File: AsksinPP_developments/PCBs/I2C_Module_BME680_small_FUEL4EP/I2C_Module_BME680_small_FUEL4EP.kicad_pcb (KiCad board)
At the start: 2 copper layers, 14.1 x 17 mm, 11 parts, among them J1 Conn_01x04, U1 BME680

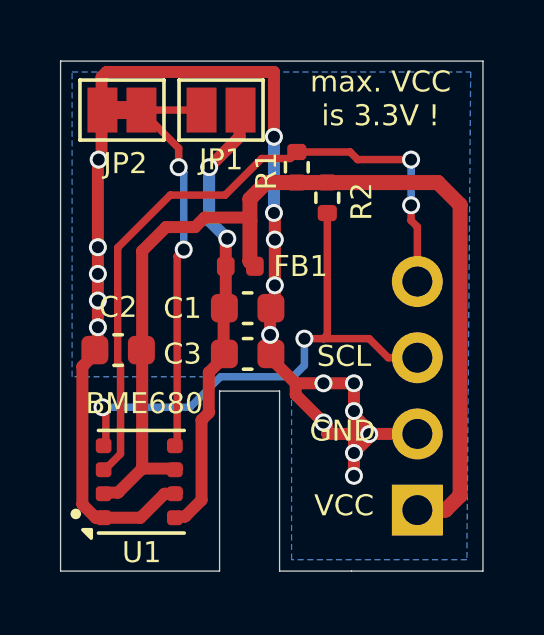
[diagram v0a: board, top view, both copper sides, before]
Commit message: PCBs: migration to KiCAD8 / PCBs/I2C_Module_BME680_small_FUEL4EP: improved VDDA decoupling
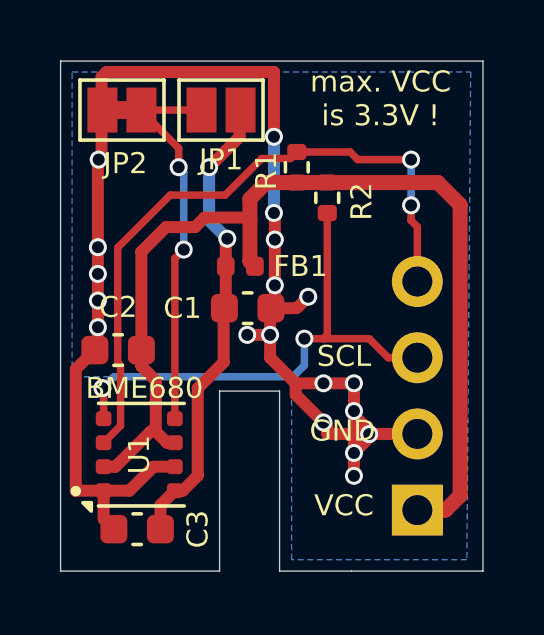
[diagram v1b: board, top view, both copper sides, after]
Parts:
- moved C3 6.91 mm to (2.55, -1.40), turned to 0 degrees
- moved U1 0.90 mm to (2.62, -3.88)
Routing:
- net GND: track 47.0 -> 49.7 mm, vias 17 -> 19
- net Net-(JP1-A): track 13.8 -> 13.0 mm
- net /SDA: track 23.0 -> 22.1 mm
- net VCC: track 35.2 -> 34.5 mm
- net VDDA: track 15.0 -> 15.6 mm
- net /SCL: track 17.8 -> 17.2 mm
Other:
- board text added: "BME680 I2C Modul small (C) FUEL4EP V1.1 09/2024"
- board text removed: "BME680 I2C Modul small (C) FUEL4EP V1.0 09/2024"

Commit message: PCBs: updated some JLCPCB manufacturing data after trial-order
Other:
- board text added: "JLCJLCJLCJLC"
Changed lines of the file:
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@@
 		(sheetfile "I2C_Module_BME680_small_FUEL4EP.kicad_sch")
 		(zone_connect 1)
-		(attr exclude_from_pos_files)
+		(attr exclude_from_pos_files exclude_from_bom)
 		(fp_line
 			(start -1.4 -1)
@@
 		(sheetfile "I2C_Module_BME680_small_FUEL4EP.kicad_sch")
 		(zone_connect 1)
-		(attr exclude_from_pos_files)
+		(attr exclude_from_pos_files exclude_from_bom)
 		(net_tie_pad_groups "1, 2")
 		(fp_poly
@@
 		)
 		(property "Value" "100n"
-			(at 0 1.43 360)
+			(at 0 1.43 0)
 			(layer "F.Fab")
 			(effects
@@
 		)
 		(fp_text user "${REFERENCE}"
-			(at 0 0 360)
+			(at 0 0 0)
 			(layer "F.Fab")
 			(effects
@@
 		(sheetname "Stammblatt")
 		(sheetfile "I2C_Module_BME680_small_FUEL4EP.kicad_sch")
-		(attr through_hole exclude_from_pos_files)
+		(attr through_hole exclude_from_pos_files exclude_from_bom)
 		(fp_line
 			(start -1.33 -8.95)
@@
 			(size 1.7 1.7)
 			(drill 1)
-			(layers "*.Cu" "*.Mask")
+			(layers "*.Cu" "*.Mask" "In1.Cu" "In2.Cu" "In3.Cu" "In4.Cu" "In5.Cu" "In6.Cu"
+				"In7.Cu" "In8.Cu" "In9.Cu" "In10.Cu" "In11.Cu" "In12.Cu" "In13.Cu" "In14.Cu"
+				"In15.Cu" "In16.Cu" "In17.Cu" "In18.Cu" "In19.Cu" "In20.Cu" "In21.Cu"
+				"In22.Cu" "In23.Cu" "In24.Cu" "In25.Cu" "In26.Cu" "In27.Cu" "In28.Cu"
+				"In29.Cu" "In30.Cu"
+			)
 			(remove_unused_layers no)
 			(net 1 "VCC")
@@
 			(size 1.7 1.7)
 			(drill 1)
-			(layers "*.Cu" "*.Mask")
+			(layers "*.Cu" "*.Mask" "In1.Cu" "In2.Cu" "In3.Cu" "In4.Cu" "In5.Cu" "In6.Cu"
+				"In7.Cu" "In8.Cu" "In9.Cu" "In10.Cu" "In11.Cu" "In12.Cu" "In13.Cu" "In14.Cu"
+				"In15.Cu" "In16.Cu" "In17.Cu" "In18.Cu" "In19.Cu" "In20.Cu" "In21.Cu"
+				"In22.Cu" "In23.Cu" "In24.Cu" "In25.Cu" "In26.Cu" "In27.Cu" "In28.Cu"
+				"In29.Cu" "In30.Cu"
+			)
 			(remove_unused_layers no)
 			(net 2 "GND")
@@
 			(size 1.7 1.7)
 			(drill 1)
-			(layers "*.Cu" "*.Mask")
+			(layers "*.Cu" "*.Mask" "In1.Cu" "In2.Cu" "In3.Cu" "In4.Cu" "In5.Cu" "In6.Cu"
+				"In7.Cu" "In8.Cu" "In9.Cu" "In10.Cu" "In11.Cu" "In12.Cu" "In13.Cu" "In14.Cu"
+				"In15.Cu" "In16.Cu" "In17.Cu" "In18.Cu" "In19.Cu" "In20.Cu" "In21.Cu"
+				"In22.Cu" "In23.Cu" "In24.Cu" "In25.Cu" "In26.Cu" "In27.Cu" "In28.Cu"
+				"In29.Cu" "In30.Cu"
+			)
 			(remove_unused_layers no)
 			(net 3 "/SCL")
@@
 			(size 1.7 1.7)
 			(drill 1)
-			(layers "*.Cu" "*.Mask")
+			(layers "*.Cu" "*.Mask" "In1.Cu" "In2.Cu" "In3.Cu" "In4.Cu" "In5.Cu" "In6.Cu"
+				"In7.Cu" "In8.Cu" "In9.Cu" "In10.Cu" "In11.Cu" "In12.Cu" "In13.Cu" "In14.Cu"
+				"In15.Cu" "In16.Cu" "In17.Cu" "In18.Cu" "In19.Cu" "In20.Cu" "In21.Cu"
+				"In22.Cu" "In23.Cu" "In24.Cu" "In25.Cu" "In26.Cu" "In27.Cu" "In28.Cu"
+				"In29.Cu" "In30.Cu"
+			)
 			(remove_unused_layers no)
 			(net 4 "/SDA")
@@
 		(sheetname "Stammblatt")
 		(sheetfile "I2C_Module_BME680_small_FUEL4EP.kicad_sch")
-		(attr through_hole)
+		(attr through_hole exclude_from_pos_files exclude_from_bom)
 		(fp_poly
 			(pts
@@
 		)
 	)
+	(gr_text "JLCJLCJLCJLC"
+		(at 8.382 -0.762 -90)
+		(layer "B.SilkS")
+		(effects
+			(font
+				(size 0.8128 0.8128)
+				(thickness 0.1524)
+				(bold yes)
+			)
+			(justify left bottom mirror)
+		)
+	)
